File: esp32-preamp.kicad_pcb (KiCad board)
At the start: 2 copper layers, 90 x 70 mm, 51 parts, among them J1 INPUT 1, J10 LFE, J11 OUT, J2 INPUT 2, J3 INPUT 3, J4 AMP PWR, J5 VOLUME, J6 TSOP382, J7 SELECT, J8 POT MOTOR, J9 PWR IN, Q1 2N3904, Q2 2N3904, Q3 2N3904, Q4 2N3904, U3 TSR0.5-2450, U4 TLV702475DBV, U5 TPS60402DBV, U7 TPS72301DBV

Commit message: Tidy footprints
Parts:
- added FB1: FerriteBead_Small, Capacitor_SMD:C_1206_3216Metric_Pad1.33x1.80mm_HandSolder, F.Cu at (70.5, 62.5)
- added FB2: FerriteBead_Small, Capacitor_SMD:C_1206_3216Metric_Pad1.33x1.80mm_HandSolder, F.Cu at (70.5, 65.9)
- added U1: ~, footprints:DW16, F.Cu at (241.0, 76.5)
- added U6: ESP32 D1 Mini, ESP32 D1 Mini:esp32-wemos-d1-mini, F.Cu at (45.0, 40.0)
- R5, R6: footprint Resistor_SMD:R_1206_3216Metric_Pad1.30x1.75mm_HandSolder -> Resistor_THT:R_Axial_Power_L20.0mm_W6.4mm_P22.40mm
- moved R5 202.2 mm to (251.0, 98.0)
- moved R6 202.0 mm to (251.0, 106.0)
- moved J11 201.4 mm to (221.5, 104.5)
- moved J1 199.1 mm to (219.6, 78.6)
- moved J2 199.1 mm to (219.6, 86.4)
- moved J3 199.1 mm to (219.6, 94.2)
- moved K1 197.4 mm to (220.6, 53.9)
- moved K4 197.4 mm to (256.8, 53.9)
- moved K2 197.4 mm to (232.7, 53.9)
- moved K3 197.4 mm to (244.7, 53.9)
- moved J10 192.4 mm to (224.0, 119.4)
- moved U4 107.3 mm to (147.7, 34.5)
- moved J9 100.9 mm to (115.0, 35.5)
- moved U7 88.4 mm to (156.9, 35.0)
- moved R1 76.1 mm to (73.9, 21.3)
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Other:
- board size 90 x 70 mm -> 120 x 70 mm

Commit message: Update esp32-preamp.kicad_pcb
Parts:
- removed R10, R11, R9: 10K, Resistor_SMD:R_1206_3216Metric_Pad1.30x1.75mm_HandSolder
- R5, R6: footprint Resistor_THT:R_Axial_Power_L20.0mm_W6.4mm_P22.40mm -> Resistor_THT:R_Axial_Power_L38.0mm_W9.0mm_P40.64mm
- moved C9 83.1 mm to (143.0, 42.0)
- moved C10 78.7 mm to (148.5, 41.8)
- moved C11 78.7 mm to (148.5, 45.1)
- moved C12 78.7 mm to (148.5, 48.5)
- moved U3 54.0 mm to (134.5, 89.5)
- moved J6 20.0 mm to (19.5, 74.2)
- moved J9 17.9 mm to (131.0, 43.5)
- moved R5 15.9 mm to (235.2, 96.5)
- moved R6 15.8 mm to (235.2, 107.0)
- moved C7 10.4 mm to (95.0, 32.0)
- moved C8 9.67 mm to (95.0, 41.0)
- moved U6 9.50 mm to (35.5, 40.0)
- moved J5 6.73 mm to (48.1, 74.2)
- moved J7 6.73 mm to (31.5, 74.0)
- moved U1 1.95 mm to (241.0, 74.6)

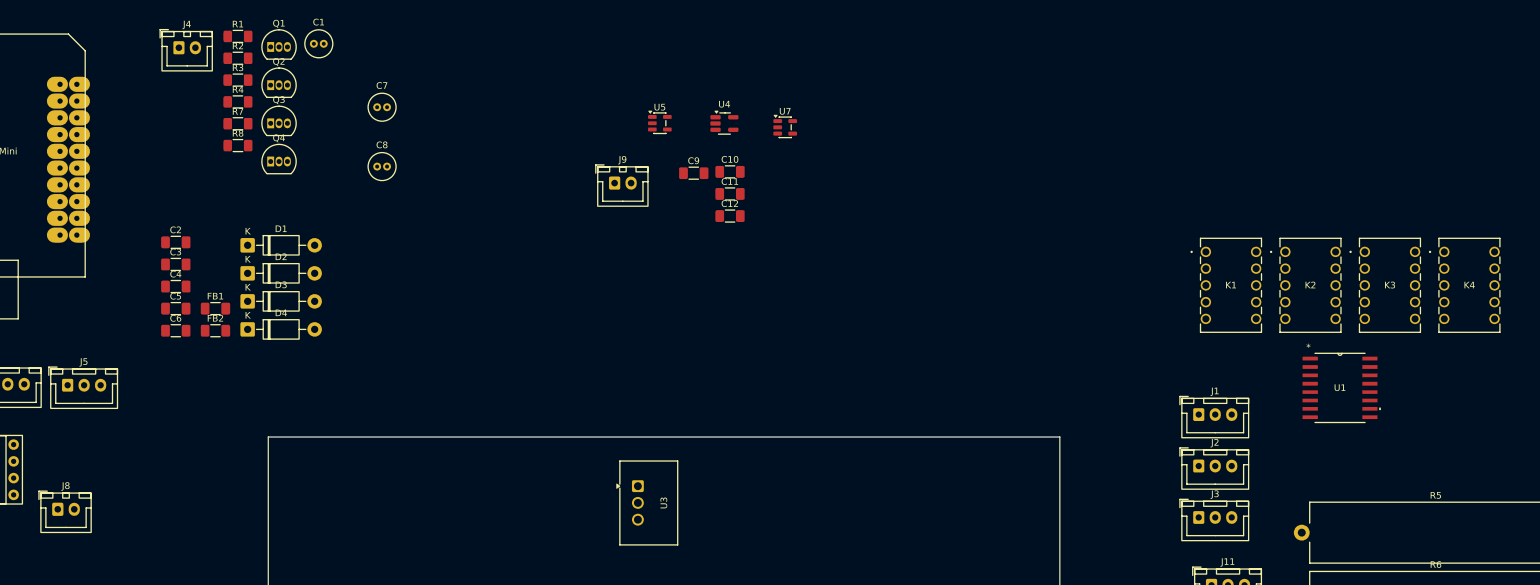
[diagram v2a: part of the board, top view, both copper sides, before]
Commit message: Group footprints
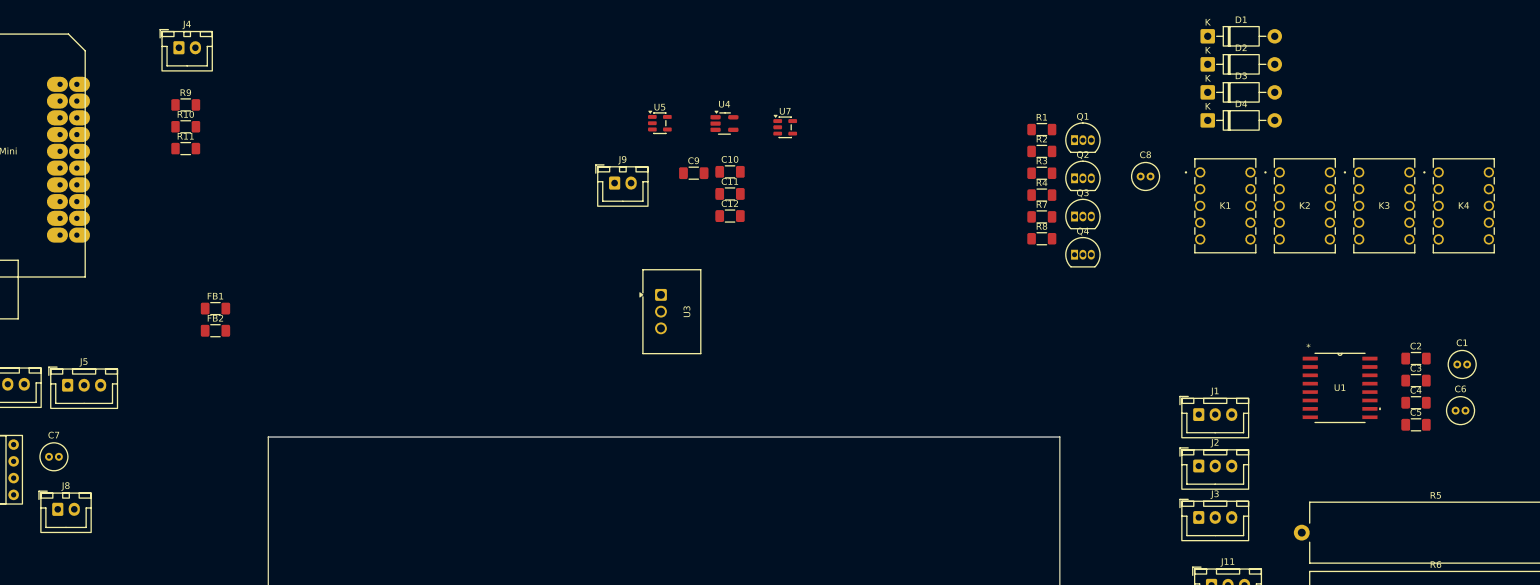
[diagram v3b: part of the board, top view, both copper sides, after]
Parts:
- added R10: 10K, Resistor_SMD:R_1206_3216Metric_Pad1.30x1.75mm_HandSolder, F.Cu at (66.0, 35.0)
- added R11: 10K, Resistor_SMD:R_1206_3216Metric_Pad1.30x1.75mm_HandSolder, F.Cu at (66.0, 38.3)
- added R9: 10K, Resistor_SMD:R_1206_3216Metric_Pad1.30x1.75mm_HandSolder, F.Cu at (66.0, 31.7)
- C6: footprint Capacitor_SMD:C_1206_3216Metric_Pad1.33x1.80mm_HandSolder -> Capacitor_THT:C_Radial_D4.0mm_H5.0mm_P1.50mm
- moved C6 194.4 mm to (258.5, 78.0)
- moved C2 188.8 mm to (252.5, 70.1)
- moved C3 188.8 mm to (252.5, 73.5)
- moved C4 188.8 mm to (252.5, 76.8)
- moved C5 188.8 mm to (252.5, 80.2)
- moved C1 180.0 mm to (258.8, 71.0)
- moved D1 149.0 mm to (220.9, 21.2)
- moved D2 149.0 mm to (220.9, 25.5)
- moved D3 149.0 mm to (220.9, 29.8)
- moved D4 149.0 mm to (220.9, 34.0)
- moved R1 122.7 mm to (195.8, 35.4)
- moved R2 122.7 mm to (195.8, 38.7)
- moved R3 122.7 mm to (195.8, 42.0)
- moved R4 122.7 mm to (195.8, 45.3)
- moved R7 122.7 mm to (195.8, 48.6)
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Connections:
- C7 pad 1: +12V -> (no net)
- C7 pad 2: GNDD -> (no net)
- C8 pad 1: +5VD -> (no net)
- C8 pad 2: GNDD -> (no net)

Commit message: Update esp32-preamp.kicad_pcb
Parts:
- moved D4 38.1 mm to (258.9, 36.0)
- moved J10 37.4 mm to (222.5, 82.0)
- moved J11 25.5 mm to (209.5, 82.0)
- moved D3 24.9 mm to (245.0, 36.0)
- moved J1 24.2 mm to (196.4, 71.5)
- moved J3 22.9 mm to (222.4, 71.5)
- moved J2 18.0 mm to (209.5, 71.5)
- moved D1 15.3 mm to (216.9, 36.0)
- moved D2 14.5 mm to (230.9, 36.0)
- moved C8 6.54 mm to (211.5, 36.0)
- moved K4 4.50 mm to (260.4, 41.9)
- moved K3 2.62 mm to (246.5, 41.9)
- moved K1 1.29 mm to (218.5, 42.0)
- moved K2 0.55 mm to (232.4, 41.9)
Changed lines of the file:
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@@
 	(footprint "Connector_JST:JST_XH_B3B-XH-A_1x03_P2.50mm_Vertical"
 		(layer "F.Cu")
-		(at 219.56 78.6)
+		(at 196.44 71.5)
 		(descr "JST XH series connector, B3B-XH-A (http://www.jst-mfg.com/product/pdf/eng/eXH.pdf)")
 		(tags "connector JST XH vertical")
@@
 			(at 2.5 -3.55 0)
 			(layer "F.SilkS")
+			(hide yes)
 			(effects
 				(font
@@
 		(property "Value" "INPUT 1"
 			(at 2.5 4.6 0)
-			(layer "F.Fab")
+			(layer "F.SilkS")
 			(effects
 				(font
@@
 	(footprint "Panasonic TQ2:RELAY_TQ2_PAN"
 		(layer "F.Cu")
-		(at 255.929 41.88)
+		(at 260.429 41.88)
 		(tags "TQ2-12V ")
 		(property "Reference" "K4"
@@
 	(footprint "Panasonic TQ2:RELAY_TQ2_PAN"
 		(layer "F.Cu")
-		(at 243.88 41.88)
+		(at 246.5 41.88)
 		(tags "TQ2-12V ")
 		(property "Reference" "K3"
@@
 	(footprint "Connector_JST:JST_XH_B2B-XH-A_1x02_P2.50mm_Vertical"
 		(layer "F.Cu")
-		(at 223.975 119.375)
+		(at 222.5 82)
 		(descr "JST XH series connector, B2B-XH-A (http://www.jst-mfg.com/product/pdf/eng/eXH.pdf)")
 		(tags "connector JST XH vertical")
@@
 			(at 1.25 -3.55 0)
 			(layer "F.SilkS")
+			(hide yes)
 			(effects
 				(font
@@
 		(property "Value" "LFE"
 			(at 1.25 4.6 0)
-			(layer "F.Fab")
+			(layer "F.SilkS")
 			(effects
 				(font
@@
 	(footprint "Connector_JST:JST_XH_B3B-XH-A_1x03_P2.50mm_Vertical"
 		(layer "F.Cu")
-		(at 219.56 86.4)
+		(at 209.5 71.5)
 		(descr "JST XH series connector, B3B-XH-A (http://www.jst-mfg.com/product/pdf/eng/eXH.pdf)")
 		(tags "connector JST XH vertical")
@@
 			(at 2.5 -3.55 0)
 			(layer "F.SilkS")
+			(hide yes)
 			(effects
 				(font
@@
 		(property "Value" "INPUT 2"
 			(at 2.5 4.6 0)
-			(layer "F.Fab")
+			(layer "F.SilkS")
 			(effects
 				(font
@@
 	(footprint "Capacitor_THT:C_Radial_D4.0mm_H5.0mm_P1.50mm"
 		(layer "F.Cu")
-		(at 210.75 42.5)
+		(at 211.5 36)
 		(descr "C, Radial series, Radial, pin pitch=1.50mm, diameter=4mm, height=5mm, Non-Polar Electrolytic Capacitor")
 		(tags "C Radial series Radial pin pitch 1.50mm diameter 4mm height 5mm Non-Polar Electrolytic Capacitor")
@@
 	(footprint "Diode_THT:D_DO-41_SOD81_P10.16mm_Horizontal"
 		(layer "F.Cu")
-		(at 220.92 21.25)
+		(at 216.92 36)
 		(descr "Diode, DO-41_SOD81 series, Axial, Horizontal, pin pitch=10.16mm, length*diameter=5.2*2.7mm^2, https://www.diodes.com/assets/Package-Files/DO-41-Plastic.pdf")
 		(tags "Diode DO-41_SOD81 series Axial Horizontal pin pitch 10.16mm  length 5.2mm diameter 2.7mm")
@@
 	(footprint "Panasonic TQ2:RELAY_TQ2_PAN"
 		(layer "F.Cu")
-		(at 219.782 41.88)
+		(at 218.5 42)
 		(tags "TQ2-12V ")
 		(property "Reference" "K1"
@@
 	(footprint "Diode_THT:D_DO-41_SOD81_P10.16mm_Horizontal"
 		(layer "F.Cu")
-		(at 220.92 34)
+		(at 258.92 36)
 		(descr "Diode, DO-41_SOD81 series, Axial, Horizontal, pin pitch=10.16mm, length*diameter=5.2*2.7mm^2, https://www.diodes.com/assets/Package-Files/DO-41-Plastic.pdf")
 		(tags "Diode DO-41_SOD81 series Axial Horizontal pin pitch 10.16mm  length 5.2mm diameter 2.7mm")
@@
 	(footprint "Connector_JST:JST_XH_B3B-XH-A_1x03_P2.50mm_Vertical"
 		(layer "F.Cu")
-		(at 221.5 104.475)
+		(at 209.5 82)
 		(descr "JST XH series connector, B3B-XH-A (http://www.jst-mfg.com/product/pdf/eng/eXH.pdf)")
 		(tags "connector JST XH vertical")
@@
 			(at 2.5 -3.55 0)
 			(layer "F.SilkS")
+			(hide yes)
 			(effects
 				(font
@@
 		(property "Value" "OUT"
 			(at 2.5 4.6 0)
-			(layer "F.Fab")
+			(layer "F.SilkS")
 			(effects
 				(font
@@
 	(footprint "Diode_THT:D_DO-41_SOD81_P10.16mm_Horizontal"
 		(layer "F.Cu")
-		(at 220.92 25.5)
+		(at 230.92 36)
 		(descr "Diode, DO-41_SOD81 series, Axial, Horizontal, pin pitch=10.16mm, length*diameter=5.2*2.7mm^2, https://www.diodes.com/assets/Package-Files/DO-41-Plastic.pdf")
 		(tags "Diode DO-41_SOD81 series Axial Horizontal pin pitch 10.16mm  length 5.2mm diameter 2.7mm")
@@
 	(footprint "Panasonic TQ2:RELAY_TQ2_PAN"
 		(layer "F.Cu")
-		(at 231.831 41.88)
+		(at 232.38 41.88)
 		(tags "TQ2-12V ")
 		(property "Reference" "K2"
@@
 	(footprint "Connector_JST:JST_XH_B3B-XH-A_1x03_P2.50mm_Vertical"
 		(layer "F.Cu")
-		(at 219.56 94.2)
+		(at 222.44 71.5)
 		(descr "JST XH series connector, B3B-XH-A (http://www.jst-mfg.com/product/pdf/eng/eXH.pdf)")
 		(tags "connector JST XH vertical")
@@
 			(at 2.5 -3.55 0)
 			(layer "F.SilkS")
+			(hide yes)
 			(effects
 				(font
@@
 		(property "Value" "INPUT 3"
 			(at 2.5 4.6 0)
-			(layer "F.Fab")
+			(layer "F.SilkS")
 			(effects
 				(font
@@
 	(footprint "Diode_THT:D_DO-41_SOD81_P10.16mm_Horizontal"
 		(layer "F.Cu")
-		(at 220.92 29.75)
+		(at 245.04 36)
 		(descr "Diode, DO-41_SOD81 series, Axial, Horizontal, pin pitch=10.16mm, length*diameter=5.2*2.7mm^2, https://www.diodes.com/assets/Package-Files/DO-41-Plastic.pdf")
 		(tags "Diode DO-41_SOD81 series Axial Horizontal pin pitch 10.16mm  length 5.2mm diameter 2.7mm")

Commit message: Fix J7 to reflect two input preamp
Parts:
- removed D4: 1N4004, Diode_THT:D_DO-41_SOD81_P10.16mm_Horizontal
- removed J4: AMP PWR, Connector_JST:JST_XH_B2B-XH-A_1x02_P2.50mm_Vertical
- removed K4: ~, Panasonic TQ2:RELAY_TQ2_PAN
- removed Q4: 2N3904, Package_TO_SOT_THT:TO-92_Inline
- removed R4: 1K6, Resistor_SMD:R_1206_3216Metric_Pad1.30x1.75mm_HandSolder
- removed R7: 10K, Resistor_SMD:R_1206_3216Metric_Pad1.30x1.75mm_HandSolder
- C4: footprint Capacitor_SMD:C_1206_3216Metric_Pad1.33x1.80mm_HandSolder -> Capacitor_THT:C_Radial_D4.0mm_H5.0mm_P1.50mm
- J3: value INPUT 3 -> AMP PWR; footprint Connector_JST:JST_XH_B3B-XH-A_1x03_P2.50mm_Vertical -> Connector_JST:JST_XH_B2B-XH-A_1x02_P2.50mm_Vertical
- J7: footprint Connector_JST:JST_XH_B5B-XH-A_1x05_P2.50mm_Vertical -> Connector_JST:JST_XH_B4B-XH-A_1x04_P2.50mm_Vertical
- R5, R6: footprint Resistor_THT:R_Axial_Power_L38.0mm_W9.0mm_P40.64mm -> Resistor_THT:R_Axial_Power_L30.0mm_W9.0mm_P36.4mm
- U4: footprint Package_TO_SOT_SMD:SOT-23-5_HandSoldering -> Package_TO_SOT_SMD:SOT-23-5
- U6: footprint ESP32 D1 Mini:esp32-wemos-d1-mini -> esp32-wemos-d1-mini:esp32-wemos-d1-mini
- moved C1 148.0 mm to (126.0, 136.5)
- moved C2 138.7 mm to (131.0, 137.0), turned to -90 degrees
- moved D3 133.4 mm to (137.2, 114.5), turned to 180 degrees
- moved K3 129.2 mm to (135.8, 108.5), turned to 180 degrees
- moved C8 125.6 mm to (113.0, 114.0)
- moved C3 120.4 mm to (150.5, 137.5), turned to -90 degrees
- moved C6 117.4 mm to (153.5, 130.4)
- moved U1 116.3 mm to (141.0, 134.0)
- moved C4 116.1 mm to (153.5, 137.5)
- moved C5 113.8 mm to (150.5, 130.5), turned to 90 degrees
- moved Q1 112.3 mm to (119.0, 114.0)
- moved D2 111.7 mm to (151.5, 114.5), turned to 180 degrees
- moved U5 110.7 mm to (134.9, 145.1)
- moved U4 110.5 mm to (146.5, 145.0)
- moved U7 109.9 mm to (156.0, 144.9)
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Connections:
- C7 pad 1: (no net) -> +12V
- C7 pad 2: (no net) -> GNDD
- C8 pad 1: (no net) -> +5VD
- C8 pad 2: (no net) -> GNDD
- K1 pad 3: IN_L -> IN_R
- K1 pad 4: Net-(J1-Pin_1) -> Net-(J1-Pin_2)
- K1 pad 7: Net-(J1-Pin_2) -> Net-(J1-Pin_1)
- K1 pad 8: IN_R -> IN_L
- K2 pad 3: IN_L -> IN_R
- K2 pad 4: Net-(J2-Pin_1) -> Net-(J2-Pin_2)
- K2 pad 7: Net-(J2-Pin_2) -> Net-(J2-Pin_1)
- K2 pad 8: IN_R -> IN_L
- K3 pad 3: IN_L -> unconnected-(K3-COM1-Pad3)
- K3 pad 4: Net-(J3-Pin_1) -> unconnected-(K3-NO1-Pad4)
- K3 pad 7: Net-(J3-Pin_2) -> Net-(J3-Pin_1)
- K3 pad 8: IN_R -> Net-(J3-Pin_2)
- R3 pad 1: INPUT_3 -> AMP_PWR
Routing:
- net -5VA: track 0.00 -> 30.4 mm
- net +5VA: track 0.00 -> 22.7 mm
- net Net-(J3-Pin_2): track 0.00 -> 19.3 mm
- net +5VD: track 0.00 -> 17.0 mm
- net Net-(J3-Pin_1): track 0.00 -> 15.8 mm
- net +12V: track 0.00 -> 6.57 mm
- net Net-(D3-A): track 0.00 -> 6.49 mm
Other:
- board size 120 x 70 mm -> 126 x 68 mm

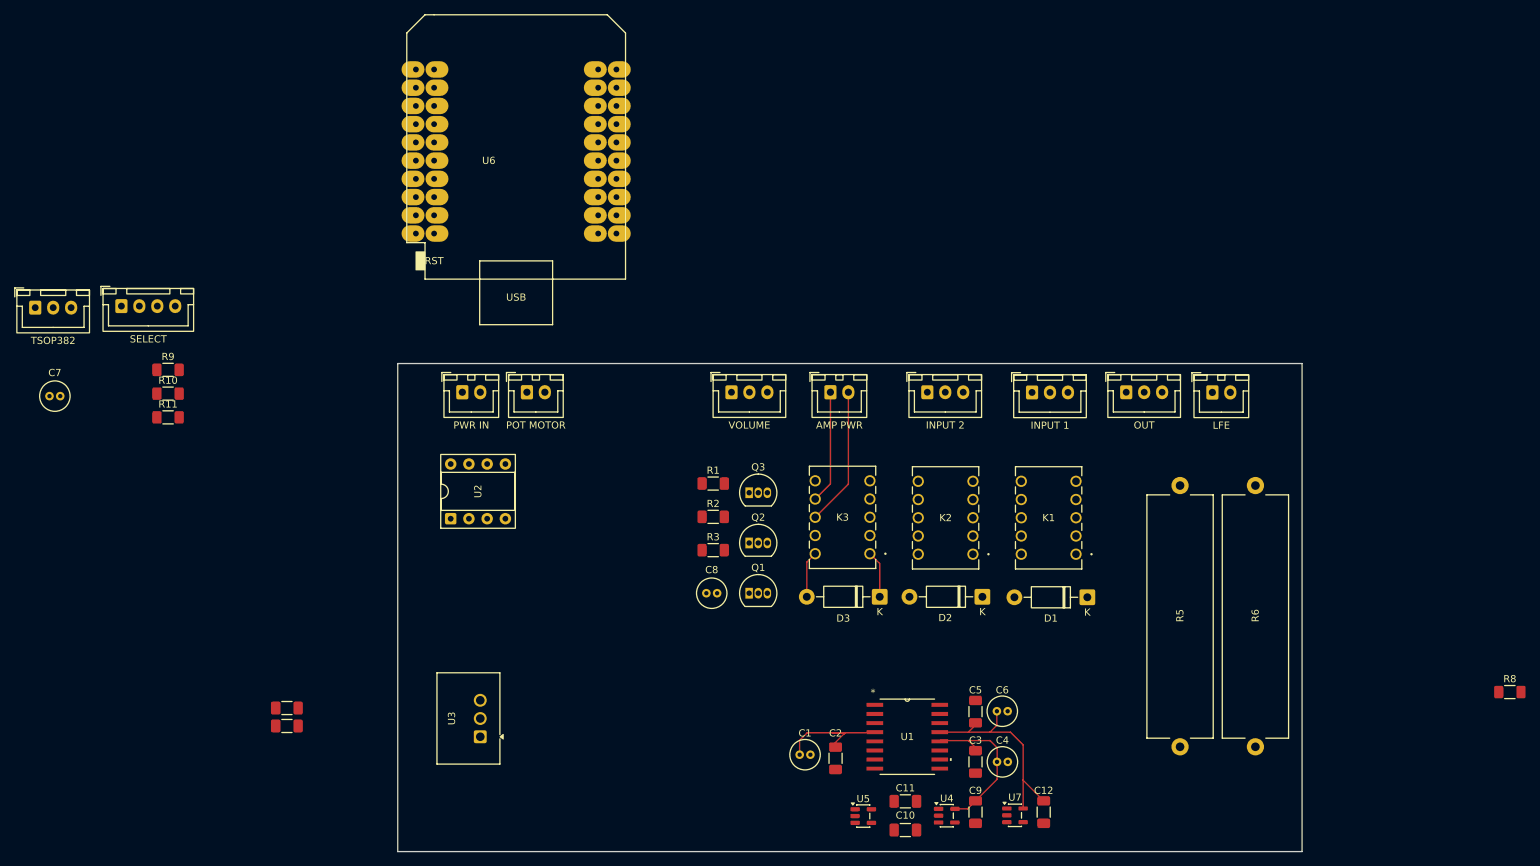
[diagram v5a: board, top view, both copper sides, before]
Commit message: Move relay capacitor
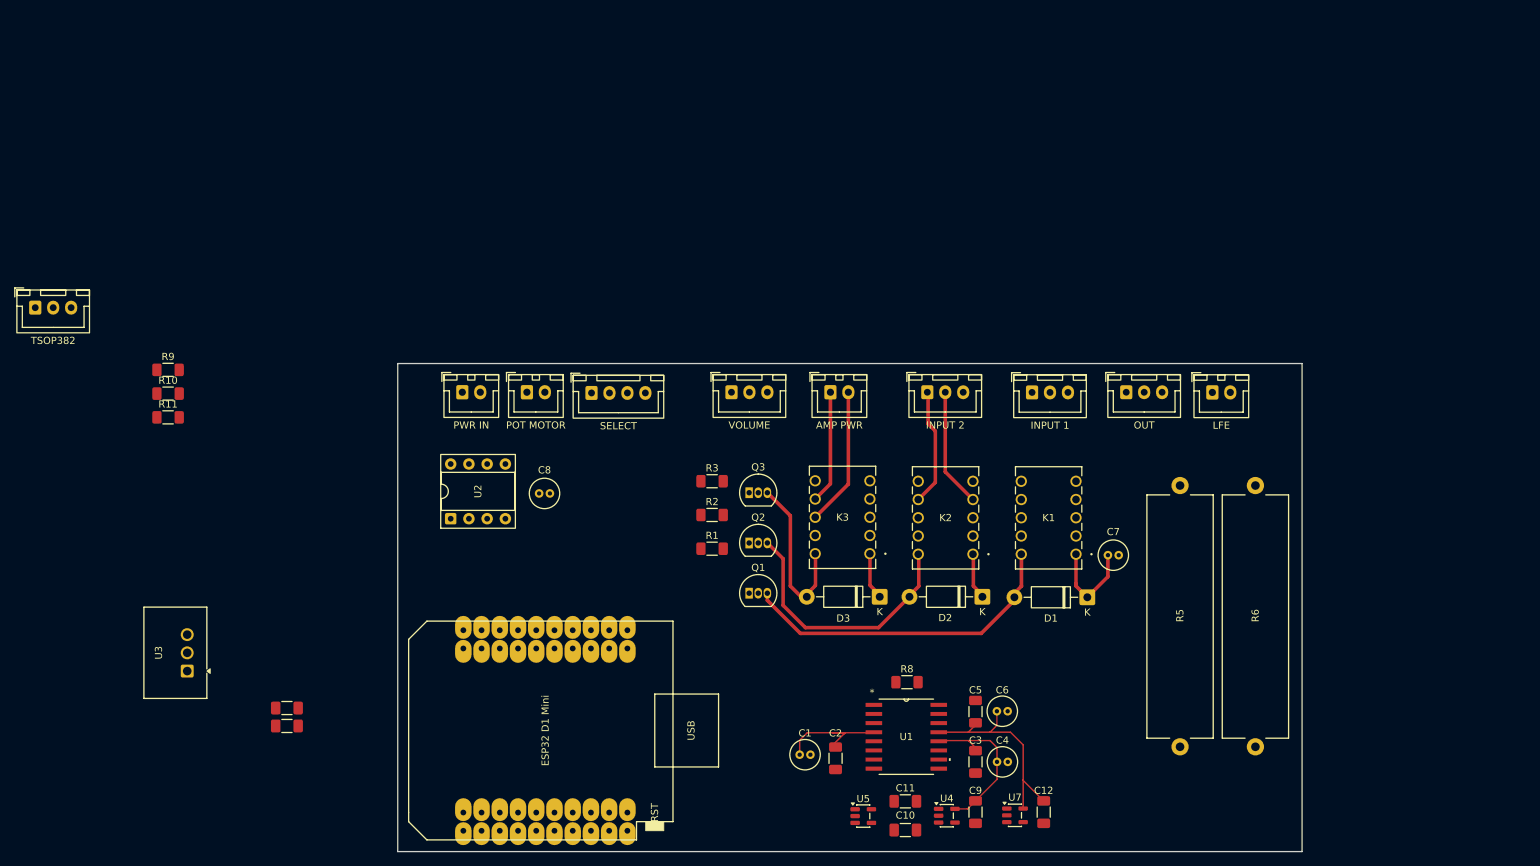
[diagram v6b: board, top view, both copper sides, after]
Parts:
- moved C7 149.1 mm to (168.9, 108.7)
- moved R8 84.0 mm to (140.9, 126.4)
- moved U6 80.8 mm to (90.6, 133.1), turned to 90 degrees
- moved J7 66.6 mm to (97.0, 86.1)
- moved U3 41.8 mm to (40.7, 124.8)
- moved C8 27.1 mm to (89.7, 100.1)
- moved R3 9.60 mm to (113.8, 98.4)
- moved R1 9.08 mm to (113.8, 107.8)
- moved R2 0.30 mm to (113.8, 103.1)
- moved U1 0.14 mm to (140.9, 134.0)
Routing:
- net Net-(D1-A): track 0.00 -> 46.2 mm
- net Net-(D2-A): track 0.00 -> 36.8 mm
- net +12V: track 6.57 -> 27.0 mm
- net Net-(D3-A): track 6.49 -> 23.8 mm
- net Net-(J2-Pin_2): track 0.00 -> 16.5 mm
- net Net-(J2-Pin_1): track 0.00 -> 16.4 mm

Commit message: Update esp32-preamp.kicad_pcb
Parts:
- moved J5 66.6 mm to (53.5, 107.6)
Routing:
- net Net-(J1-Pin_2): track 0.00 -> 16.5 mm
- net Net-(J1-Pin_1): track 0.00 -> 16.2 mm
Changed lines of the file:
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@@
 	(footprint "Connector_JST:JST_XH_B3B-XH-A_1x03_P2.50mm_Vertical"
 		(layer "F.Cu")
-		(at 116.5 86)
+		(at 53.5 107.6)
 		(descr "JST XH series connector, B3B-XH-A (http://www.jst-mfg.com/product/pdf/eng/eXH.pdf)")
 		(tags "connector JST XH vertical")
@@
 	)
 	(segment
+		(start 159.35655 98.52345)
+		(end 159.35655 91.3527)
+		(width 0.5)
+		(layer "F.Cu")
+		(net "Net-(J1-Pin_1)")
+	)
+	(segment
+		(start 156.98 100.9)
+		(end 159.35655 98.52345)
+		(width 0.5)
+		(layer "F.Cu")
+		(net "Net-(J1-Pin_1)")
+	)
+	(segment
+		(start 159.35655 91.3527)
+		(end 158.35655 90.3527)
+		(width 0.5)
+		(layer "F.Cu")
+		(net "Net-(J1-Pin_1)")
+	)
+	(segment
+		(start 158.35655 90.3527)
+		(end 158.35655 86.0658)
+		(width 0.5)
+		(layer "F.Cu")
+		(net "Net-(J1-Pin_1)")
+	)
+	(segment
+		(start 160.74345 97.04345)
+		(end 164.6 100.9)
+		(width 0.5)
+		(layer "F.Cu")
+		(net "Net-(J1-Pin_2)")
+	)
+	(segment
+		(start 160.74345 85.9527)
+		(end 160.74345 97.04345)
+		(width 0.5)
+		(layer "F.Cu")
+		(net "Net-(J1-Pin_2)")
+	)
+	(segment
